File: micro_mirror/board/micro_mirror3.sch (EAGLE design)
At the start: 139 parts, among them IC1 74LV7014, IC2 74LV02, IC3 74LV08, IC4 LM324D, IC5 LM324D, J1 POWER_JACKPTH_LOCK, U8 TPS62160, X1 SMA-142-0701-801/806, X2 SMA-142-0701-801/806, X3 SMA-142-0701-801/806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

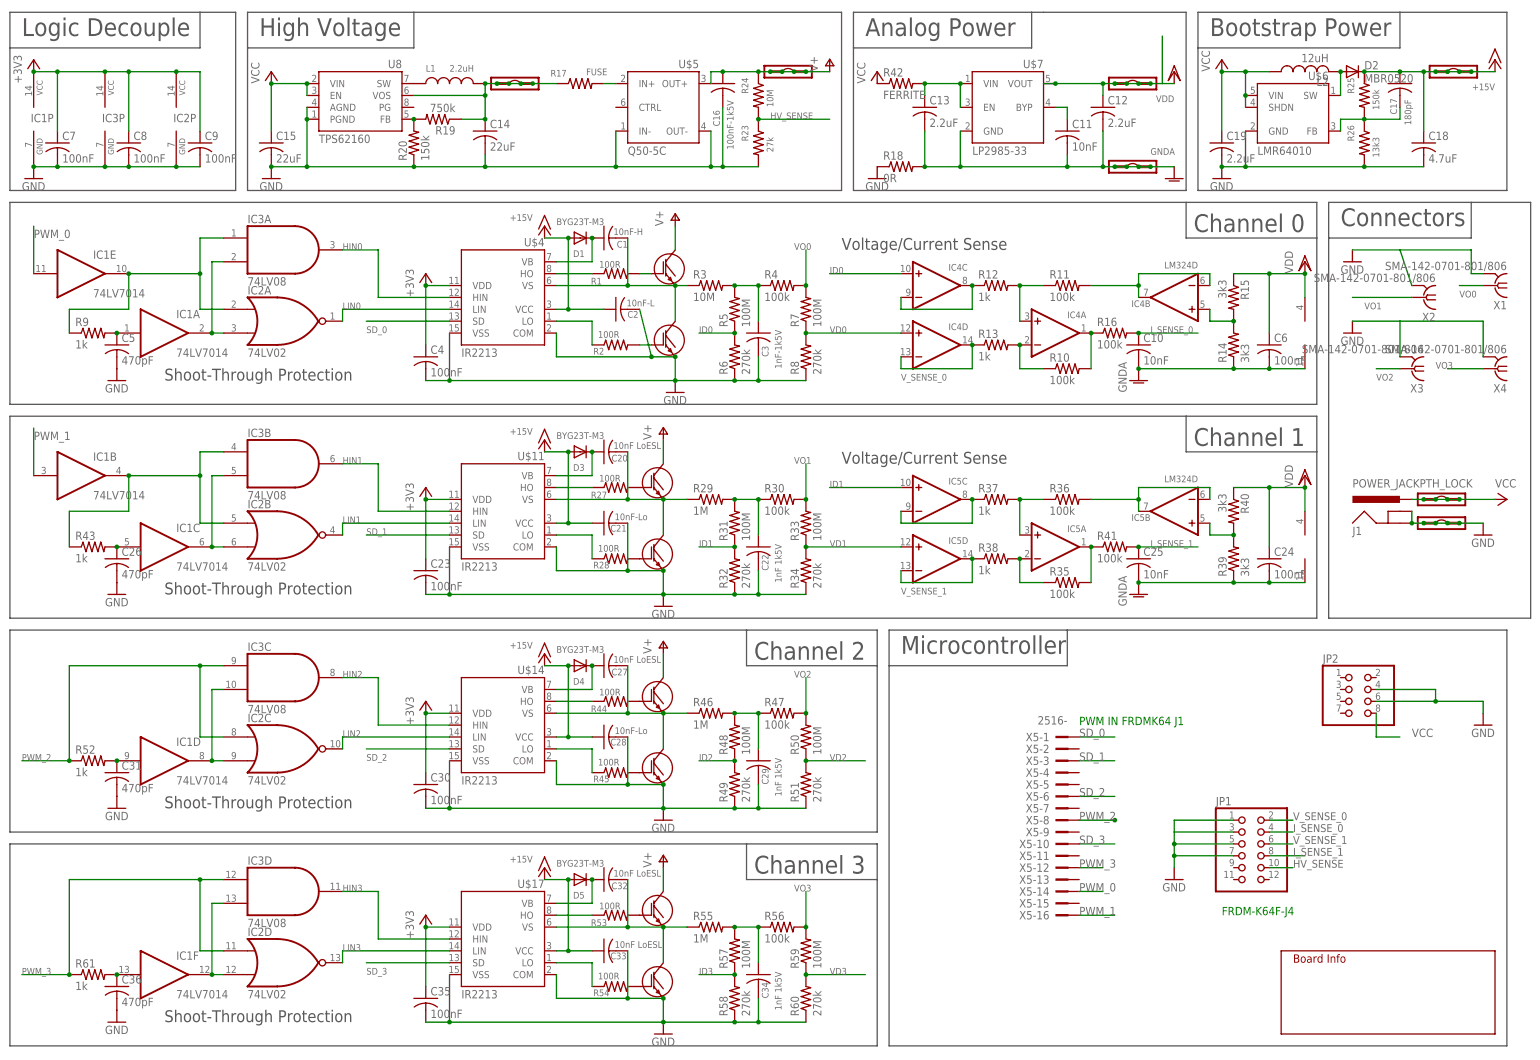
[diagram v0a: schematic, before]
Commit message: added mounting holes, and some extra libraries in common
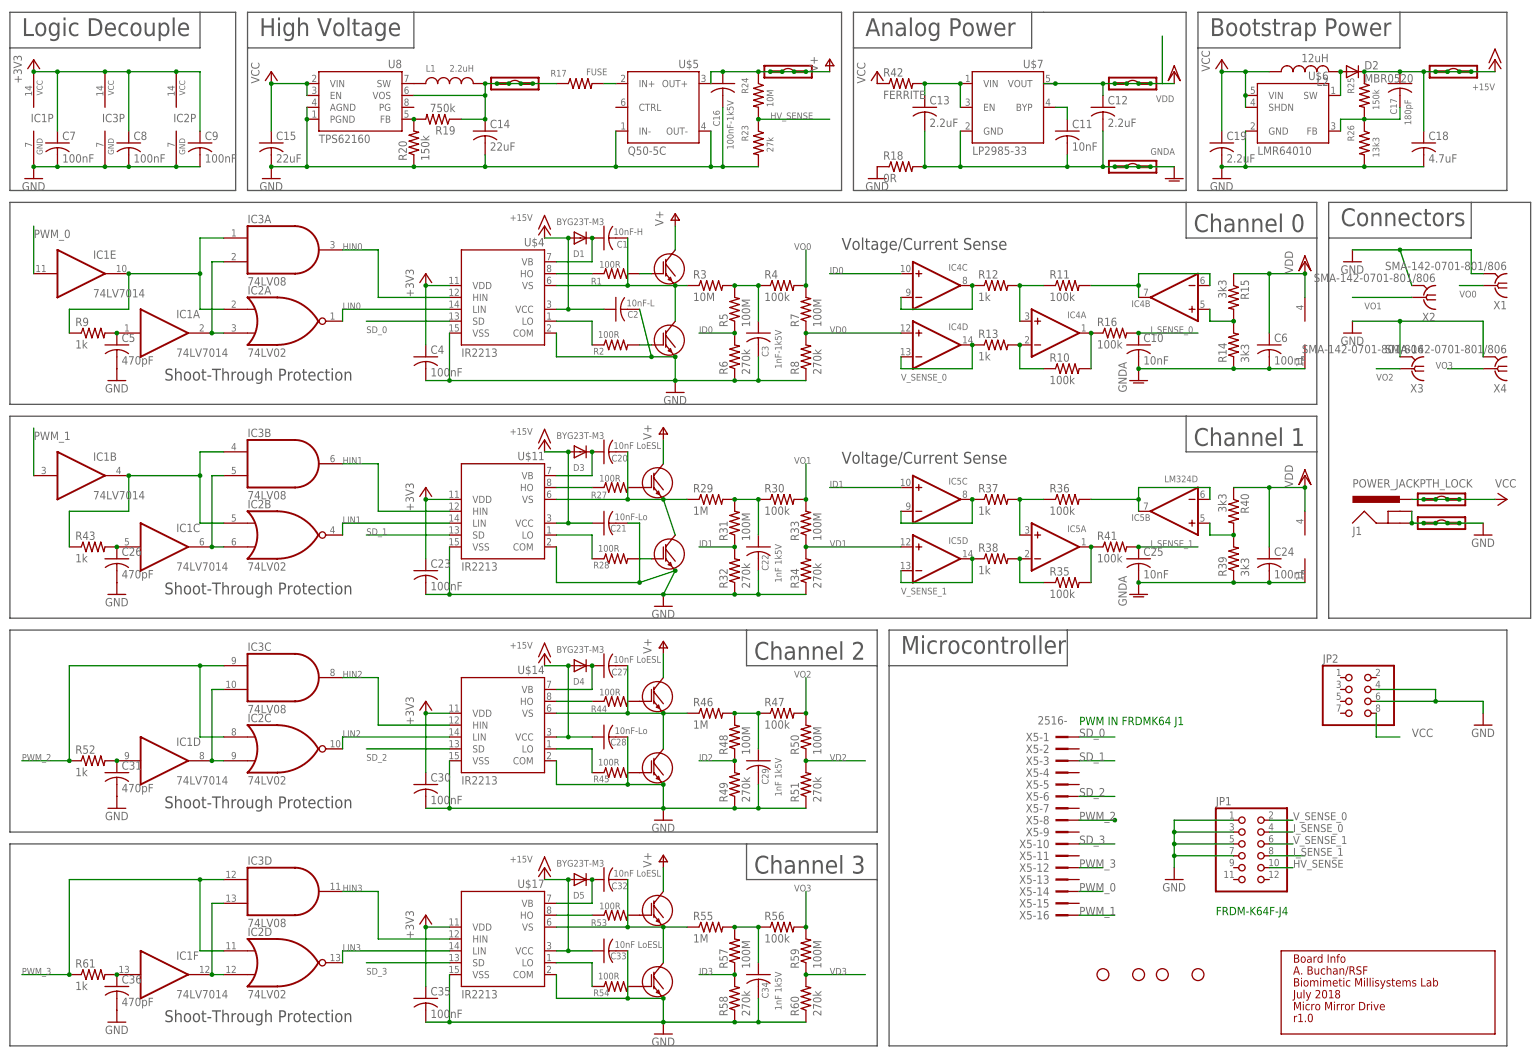
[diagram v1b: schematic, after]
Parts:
- added H5, H6, H7, H8: STAND-OFFTIGHT, SparkFun-Hardware:STAND-OFFTIGHT
- IC4: value LM324D -> (none); device linear:LM324D -> micro_mirror3:LINEAR_LM324D
- U$18: AUTHOR A. Buchan -> A. Buchan/RSF; DATE Oct. 13, 2016 -> July 2018; REVISION r0.0 -> r1.0

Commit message: started digikey BOM. consolidated resistor values for ease of assembly.
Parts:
- IC4: VERSION (none) -> LMV324
- R19: value 750k -> 510k
- R20, R25: value 150k -> 100k
- R23: value 27k -> 270k
- R24: value 10M -> 100M
- R26: value 13k3 -> 10k
- R29, R46, R55: value 1M -> 10M
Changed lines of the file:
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@@
 <part name="C5" library="rcl" deviceset="C-US" device="C1206" value="470pF"/>
 <part name="GND2" library="supply1" deviceset="GND" device=""/>
-<part name="IC4" library="micro_mirror3" deviceset="LINEAR_LM324" device="D"/>
+<part name="IC4" library="micro_mirror3" deviceset="LINEAR_LM324" device="D">
+<attribute name="VERSION" value="LMV324"/>
+</part>
 <part name="R10" library="rcl" deviceset="R-US_" device="R1206" value="100k"/>
 <part name="R11" library="rcl" deviceset="R-US_" device="R1206" value="100k"/>
@@
 <part name="GND8" library="supply1" deviceset="GND" device=""/>
 <part name="GNDA" library="modular_robotics" deviceset="M04" device="LOCK"/>
-<part name="R19" library="rcl" deviceset="R-US_" device="R1206" value="750k"/>
-<part name="R20" library="rcl" deviceset="R-US_" device="R1206" value="150k"/>
+<part name="R19" library="rcl" deviceset="R-US_" device="R1206" value="510k"/>
+<part name="R20" library="rcl" deviceset="R-US_" device="R1206" value="100k"/>
 <part name="C14" library="rcl" deviceset="C-US" device="C1206" value="22uF"/>
 <part name="C15" library="rcl" deviceset="C-US" device="C1206" value="22uF"/>
@@
 <part name="P+4" library="supply1" deviceset="VCC" device=""/>
 <part name="HV_IN" library="modular_robotics" deviceset="M04" device="LOCK"/>
-<part name="R23" library="rcl" deviceset="R-US_" device="R1206" value="27k"/>
-<part name="R24" library="rcl" deviceset="R-US_" device="R1206" value="10M"/>
+<part name="R23" library="rcl" deviceset="R-US_" device="R1206" value="270k"/>
+<part name="R24" library="rcl" deviceset="R-US_" device="R1206" value="100M"/>
 <part name="C16" library="rcl" deviceset="C-US" device="C2225K" value="100nF-1k5V"/>
 <part name="P+5" library="supply1" deviceset="V+" device=""/>
@@
 <part name="L2" library="rcl" deviceset="L-US" device="L1812" value="12uH"/>
 <part name="D2" library="diode" deviceset="DIODE-" device="SOD123" value="MBR0520"/>
-<part name="R25" library="rcl" deviceset="R-US_" device="R1206" value="150k"/>
-<part name="R26" library="rcl" deviceset="R-US_" device="R1206" value="13k3"/>
+<part name="R25" library="rcl" deviceset="R-US_" device="R1206" value="100k"/>
+<part name="R26" library="rcl" deviceset="R-US_" device="R1206" value="10k"/>
 <part name="C17" library="rcl" deviceset="C-US" device="C1206" value="180pF"/>
 <part name="C18" library="rcl" deviceset="C-US" device="C1206" value="4.7uF"/>
@@
 <part name="P+11" library="supply1" deviceset="V+" device=""/>
 <part name="GND12" library="supply1" deviceset="GND" device=""/>
-<part name="R29" library="rcl" deviceset="R-US_" device="R1206" value="1M"/>
+<part name="R29" library="rcl" deviceset="R-US_" device="R1206" value="10M"/>
 <part name="C22" library="rcl" deviceset="C-US" device="C1206" value="1nF 1k5V"/>
 <part name="R30" library="rcl" deviceset="R-US_" device="R1206" value="100k"/>
@@
 <part name="P+13" library="supply1" deviceset="V+" device=""/>
 <part name="GND16" library="supply1" deviceset="GND" device=""/>
-<part name="R46" library="rcl" deviceset="R-US_" device="R1206" value="1M"/>
+<part name="R46" library="rcl" deviceset="R-US_" device="R1206" value="10M"/>
 <part name="C29" library="rcl" deviceset="C-US" device="C1206" value="1nF 1k5V"/>
 <part name="R47" library="rcl" deviceset="R-US_" device="R1206" value="100k"/>
@@
 <part name="P+15" library="supply1" deviceset="V+" device=""/>
 <part name="GND19" library="supply1" deviceset="GND" device=""/>
-<part name="R55" library="rcl" deviceset="R-US_" device="R1206" value="1M"/>
+<part name="R55" library="rcl" deviceset="R-US_" device="R1206" value="10M"/>
 <part name="C34" library="rcl" deviceset="C-US" device="C1206" value="1nF 1k5V"/>
 <part name="R56" library="rcl" deviceset="R-US_" device="R1206" value="100k"/>
@@
 <attribute name="NAME" x="269.24" y="108.585" size="1.4224" layer="95" rot="R180"/>
 <attribute name="VALUE" x="279.4" y="116.84" size="1.4224" layer="96" rot="R180"/>
+<attribute name="VERSION" x="274.32" y="109.22" size="1.778" layer="96" rot="R180" display="off"/>
 </instance>
 <instance part="IC4" gate="P" x="302.26" y="101.6"/>

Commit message: added caps to BoM
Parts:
- C17: value 180pF -> 470pF
- C18: value 4.7uF -> 2.2uF
- D2: value MBR0520 -> MBR0530
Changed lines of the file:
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@@
 <part name="HV_OUT" library="modular_robotics" deviceset="M04" device="LOCK"/>
 <part name="L2" library="rcl" deviceset="L-US" device="L1812" value="12uH"/>
-<part name="D2" library="diode" deviceset="DIODE-" device="SOD123" value="MBR0520"/>
+<part name="D2" library="diode" deviceset="DIODE-" device="SOD123" value="MBR0530"/>
 <part name="R25" library="rcl" deviceset="R-US_" device="R1206" value="100k"/>
 <part name="R26" library="rcl" deviceset="R-US_" device="R1206" value="10k"/>
-<part name="C17" library="rcl" deviceset="C-US" device="C1206" value="180pF"/>
-<part name="C18" library="rcl" deviceset="C-US" device="C1206" value="4.7uF"/>
+<part name="C17" library="rcl" deviceset="C-US" device="C1206" value="470pF"/>
+<part name="C18" library="rcl" deviceset="C-US" device="C1206" value="2.2uF"/>
 <part name="C19" library="rcl" deviceset="C-US" device="C1206" value="2.2uF"/>
 <part name="P+6" library="supply1" deviceset="+15V" device=""/>

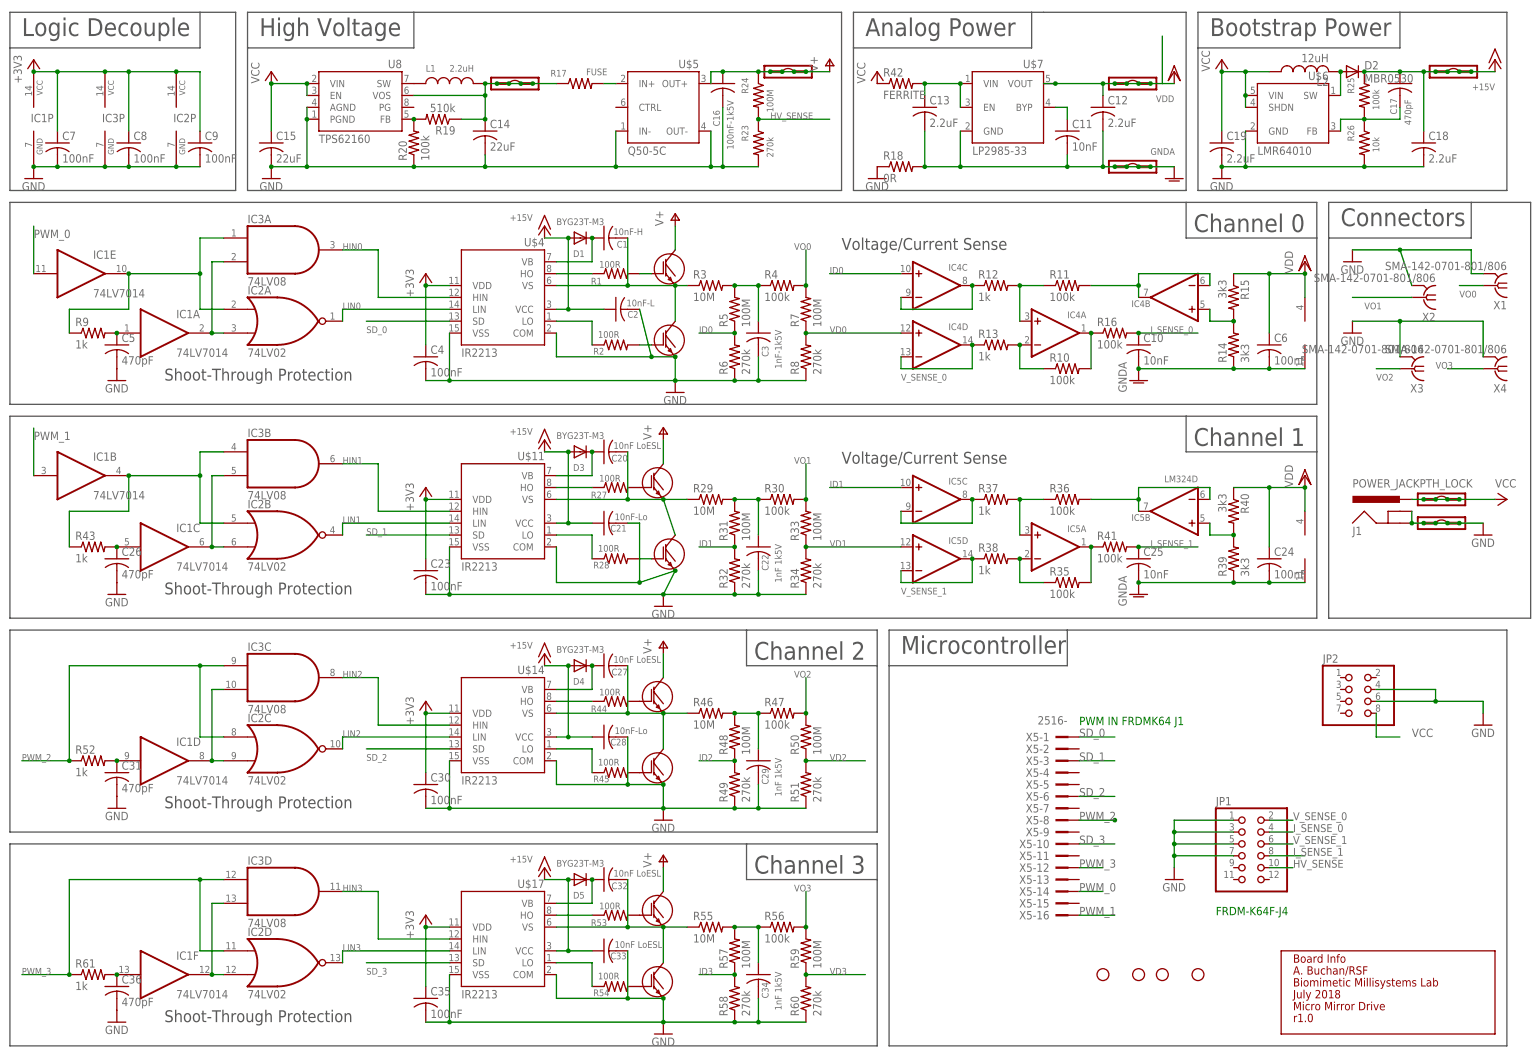
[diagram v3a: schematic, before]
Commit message: added k64F connection .pdf
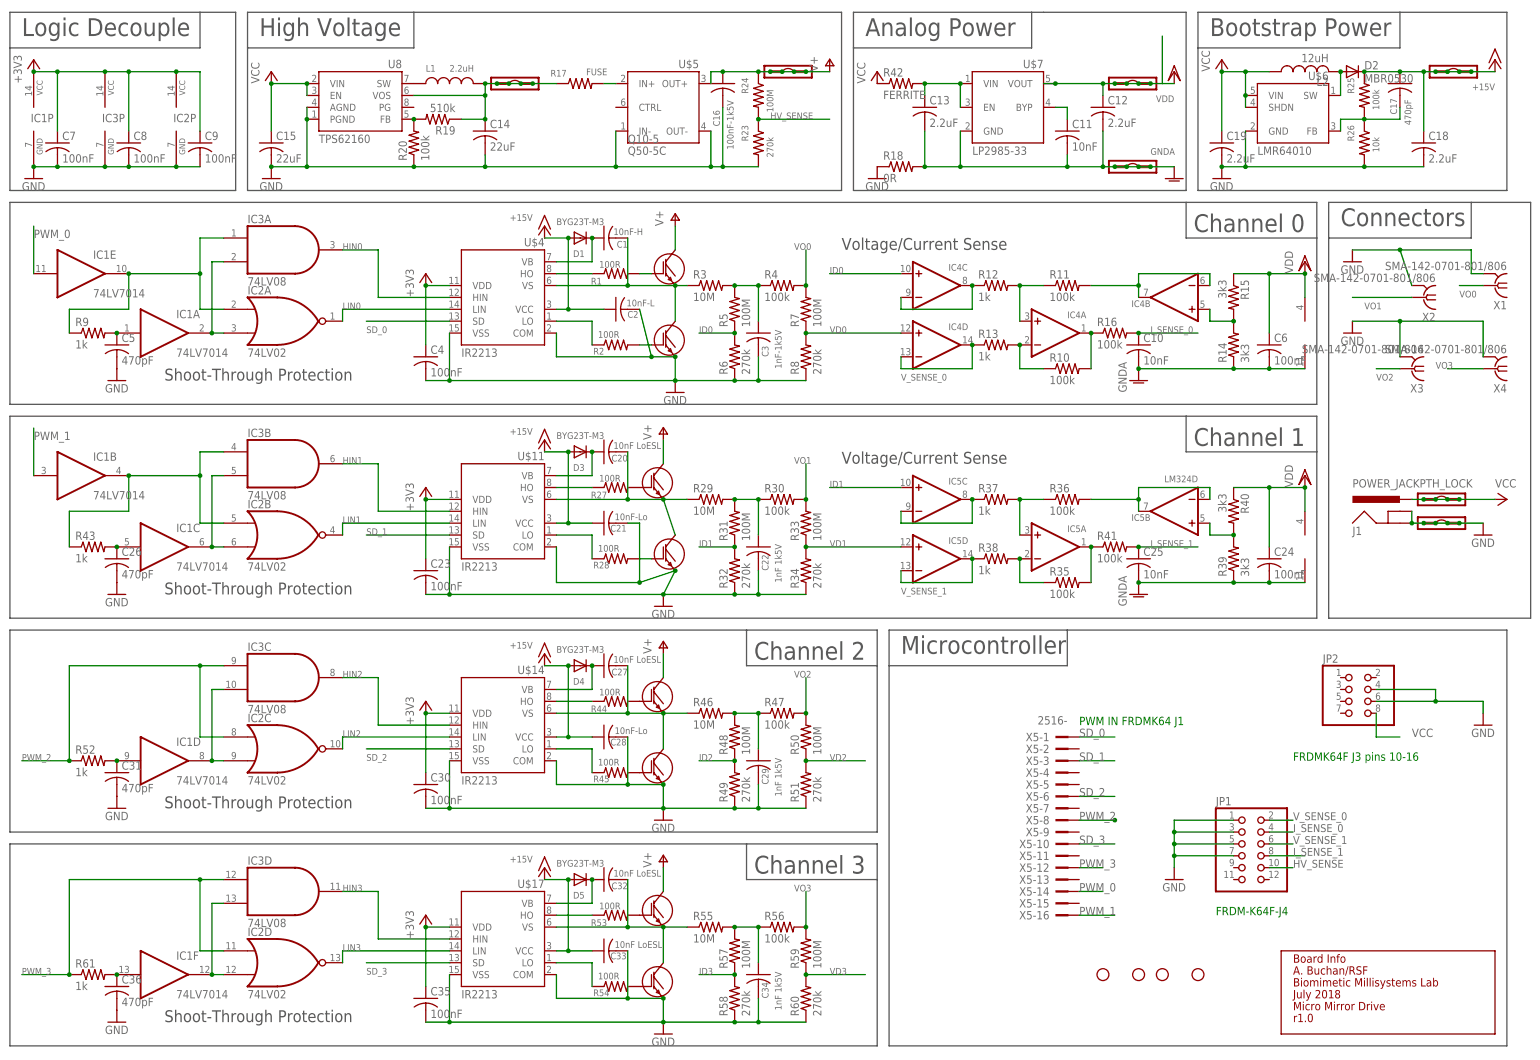
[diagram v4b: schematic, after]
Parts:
- J1: DIMENSIONS (none) -> 5.5mm-diam
- U$5: EMCO (none) -> Q10-5
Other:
- note added: "FRDMK64F J3 pins 10-16"
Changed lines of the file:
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@@
 <part name="C10" library="rcl" deviceset="C-US" device="C1206" value="10nF"/>
 <part name="GND6" library="supply1" deviceset="GNDA" device=""/>
-<part name="U$5" library="modular_robotics" deviceset="Q50-5C" device=""/>
+<part name="U$5" library="modular_robotics" deviceset="Q50-5C" device="">
+<attribute name="EMCO" value="Q10-5"/>
+</part>
 <part name="R17" library="rcl" deviceset="R-US_" device="R1206" value="FUSE"/>
 <part name="L1" library="modular_robotics" deviceset="INDUCTOR" device="" value="2.2uH"/>
@@
 <part name="P+7" library="supply1" deviceset="VCC" device=""/>
 <part name="15V_OUT" library="modular_robotics" deviceset="M04" device="LOCK"/>
-<part name="J1" library="SparkFun-Connectors" deviceset="POWER_JACK" device="PTH_LOCK"/>
+<part name="J1" library="SparkFun-Connectors" deviceset="POWER_JACK" device="PTH_LOCK">
+<attribute name="DIMENSIONS" value="5.5mm-diam"/>
+</part>
 <part name="GND11" library="supply1" deviceset="GND" device=""/>
 <part name="P+9" library="supply1" deviceset="VCC" device=""/>
@@
 <text x="254" y="17.78" size="1.778" layer="91">PWM IN FRDMK64 J1</text>
 <text x="283.21" y="-22.86" size="1.778" layer="91">FRDM-K64F-J4</text>
+<text x="299.72" y="10.16" size="1.778" layer="91">FRDMK64F J3 pins 10-16</text>
 </plain>
 <instances>
@@
 <instance part="C10" gate="G$1" x="266.7" y="99.06"/>
 <instance part="GND6" gate="1" x="266.7" y="91.44"/>
-<instance part="U$5" gate="G$1" x="157.48" y="142.24"/>
+<instance part="U$5" gate="G$1" x="157.48" y="142.24">
+<attribute name="EMCO" x="157.48" y="142.24" size="1.778" layer="96"/>
+</instance>
 <instance part="R17" gate="G$1" x="147.32" y="154.94" smashed="yes">
 <attribute name="NAME" x="140.97" y="156.4386" size="1.4224" layer="95"/>
@@
 <instance part="P+7" gate="VCC" x="284.48" y="160.02"/>
 <instance part="15V_OUT" gate="G$1" x="335.28" y="157.48" rot="R90"/>
-<instance part="J1" gate="G$1" x="322.58" y="58.42"/>
+<instance part="J1" gate="G$1" x="322.58" y="58.42">
+<attribute name="DIMENSIONS" x="322.58" y="58.42" size="1.778" layer="96" display="off"/>
+</instance>
 <instance part="GND11" gate="1" x="340.36" y="58.42"/>
 <instance part="P+9" gate="VCC" x="345.44" y="66.04" rot="R270"/>
